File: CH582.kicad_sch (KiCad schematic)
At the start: 27 parts, among them SW1 RESET, SW2 POWER, SW3 POWER, U2 XC6220B331QR-G, U3 M3406, Y1 32MHz, Y2 Crystal_Small

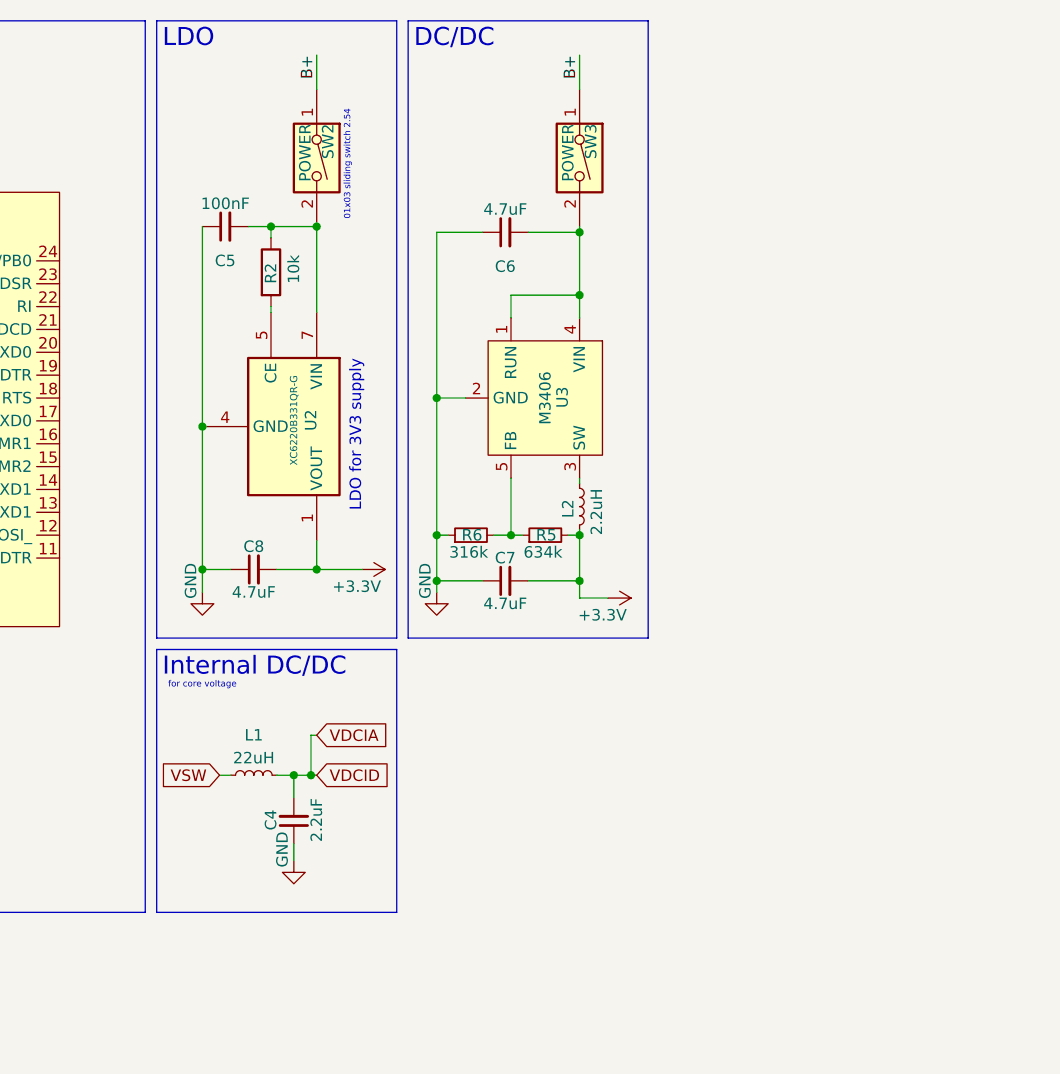
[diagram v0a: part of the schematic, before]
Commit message: added charging circuit
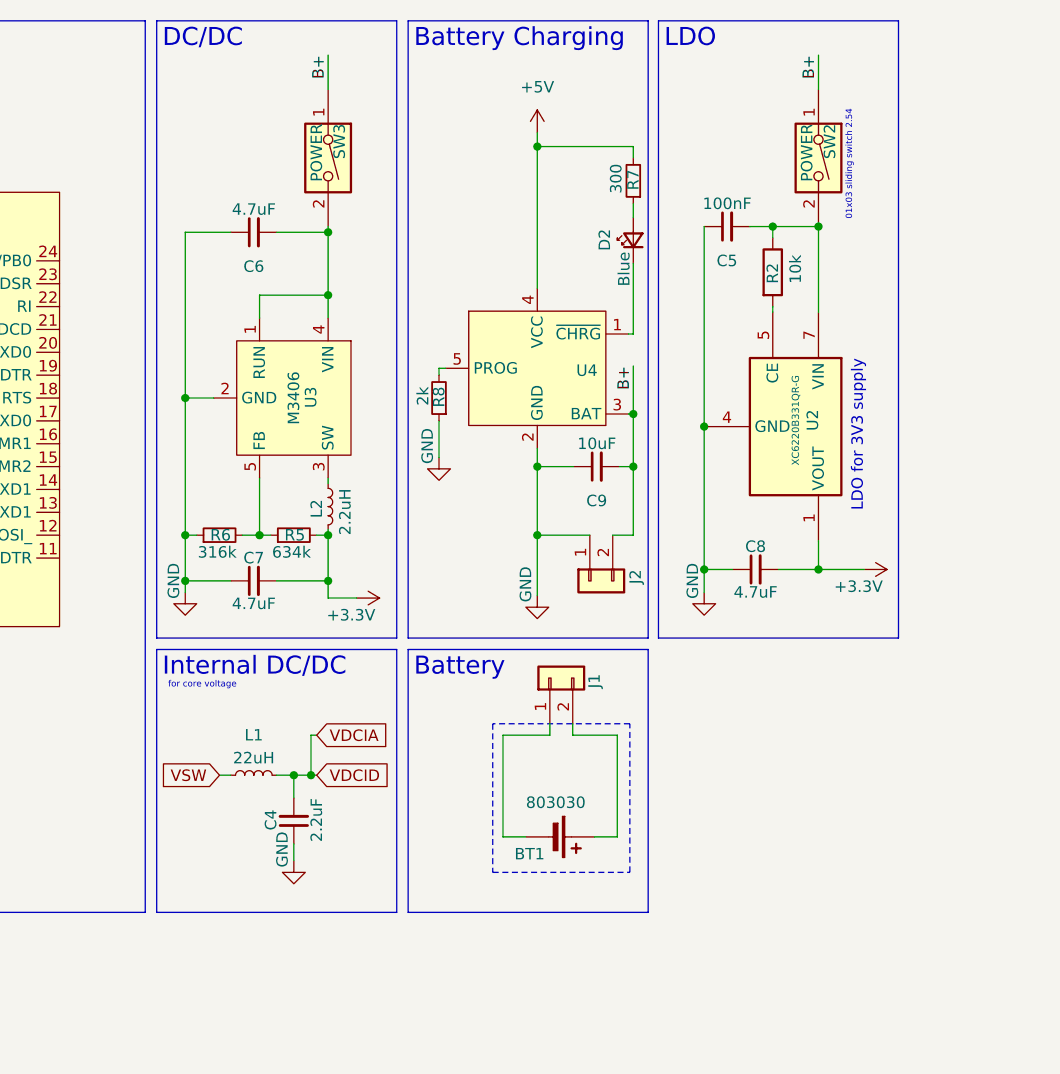
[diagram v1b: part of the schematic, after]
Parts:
- added BT1: 803030, symbol Device:Battery_Cell
- added C9: 10uF, Capacitor_SMD:C_1206_3216Metric_Pad1.33x1.80mm_HandSolder, symbol Device:C_Small
- added D2: Blue, symbol Device:LED_Small
- added J1, J2: Conn_01x02, symbol Connector_Generic:Conn_01x02
- added R7: 300, symbol Device:R_Small
- added R8: 2k, symbol Device:R_Small
- added U4: ~, symbol Custom:PJ4054B
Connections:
- net B+: now also C9.2, J2.2 (Pin_2), U4.3 (BAT)
- net GND: now also C9.1, J2.1 (Pin_1), R8.1, U4.2 (GND)
- new net: BT1.1 (+), J1.2 (Pin_2)
- new net: BT1.2 (-), J1.1 (Pin_1)
- new net: D2.2 (A), R7.1
- new net: D2.1 (K), U4.1 (~{CHRG})
- new net: R8.2, U4.5 (PROG)
- new net +5V: R7.2, U4.4 (VCC)
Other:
- note added: "Battery"
- note added: "Battery Charging"
- moved on the sheet: C5, C6, C7, C8, L2, R2, R5, R6, SW2, SW3, U2, U3

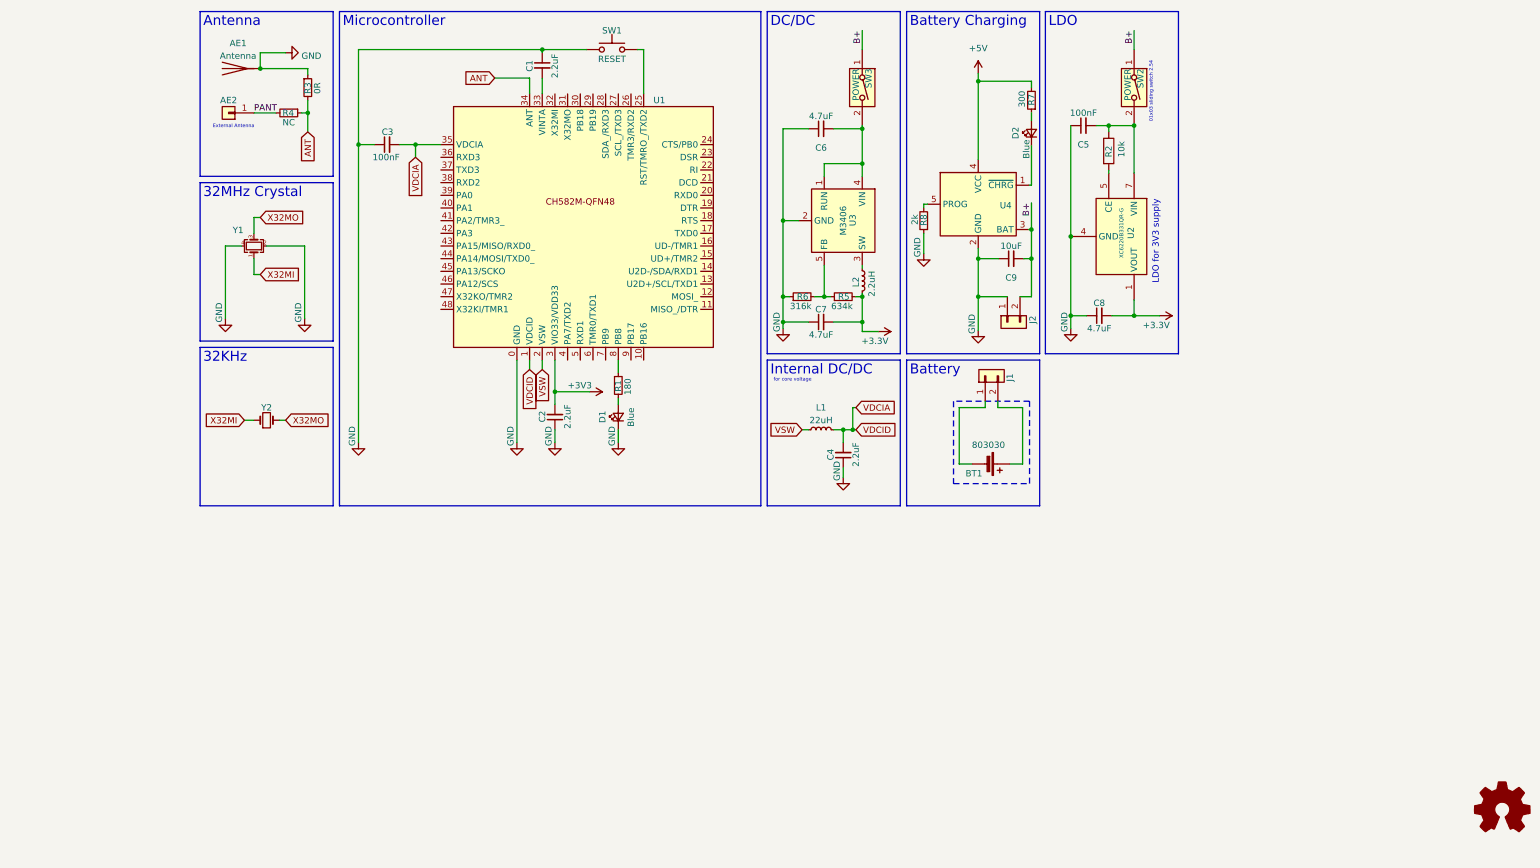
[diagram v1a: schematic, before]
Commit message: restructured layout
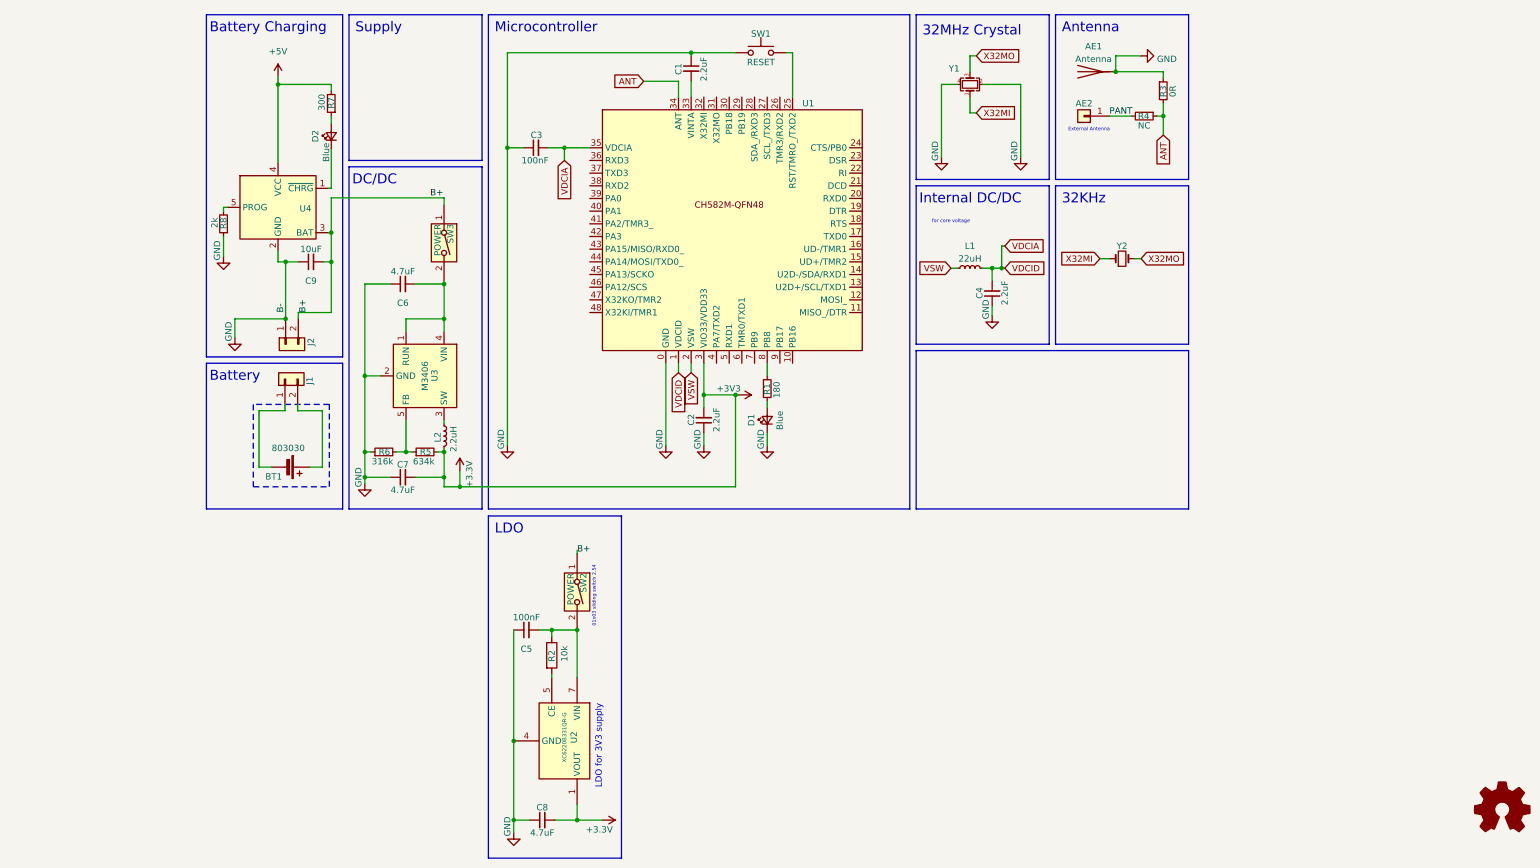
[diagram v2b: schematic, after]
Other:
- note added: "Supply"
- moved on the sheet: AE1, AE2, BT1, C1, C2, C3, C4, C5, C6, C7, C8, C9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

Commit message: Bat Lvl, GP conn, icm/lsm
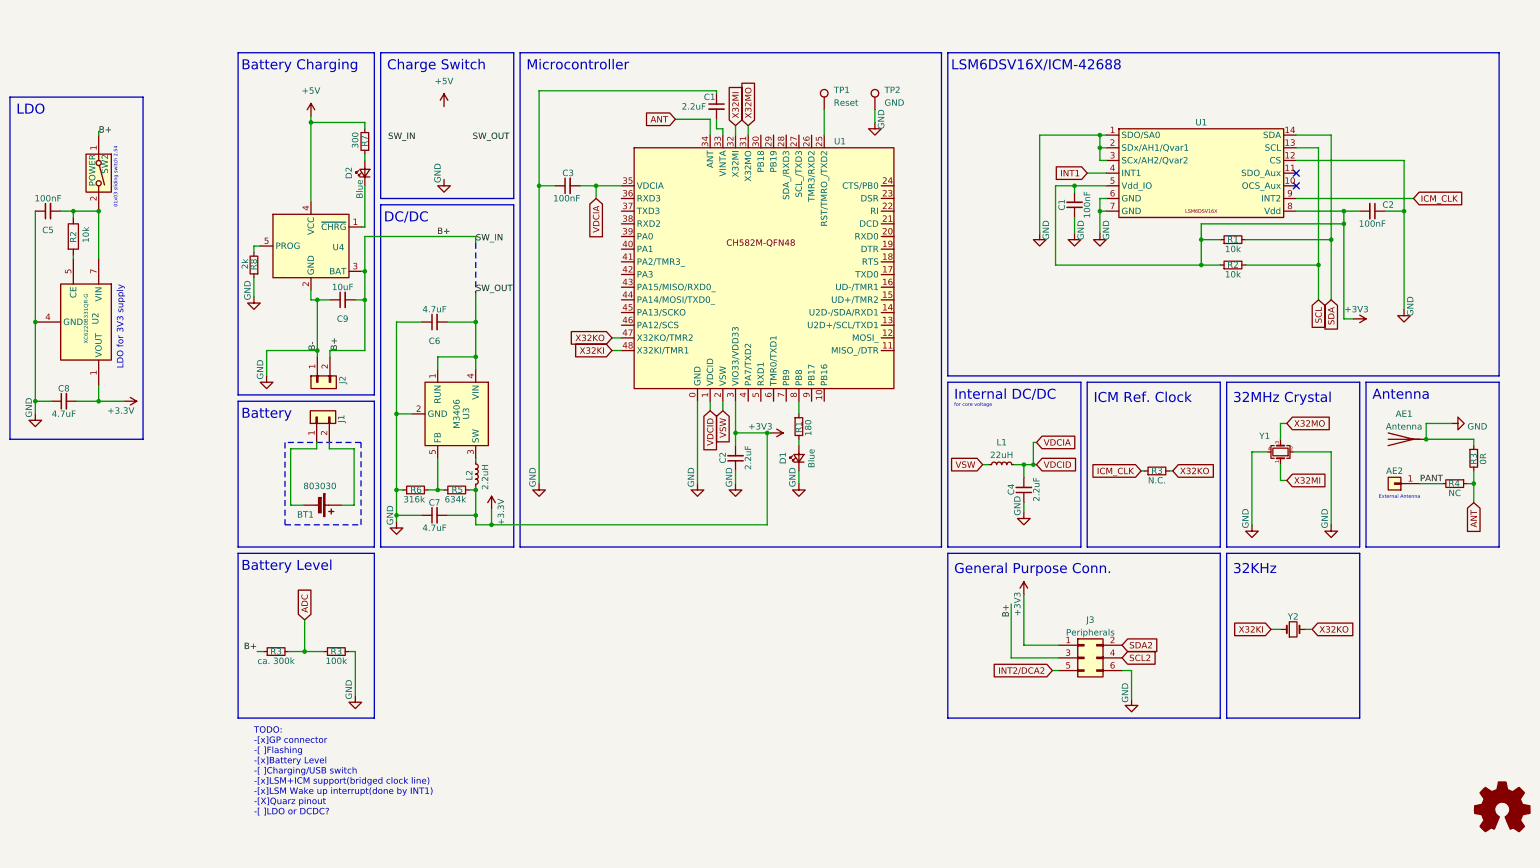
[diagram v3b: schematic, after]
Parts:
- removed SW1: RESET, symbol Switch:SW_Push
- removed SW3: POWER, Connector_PinSocket_2.54mm:PinSocket_1x03_P2.54mm_Vertical, symbol Switch:SW_DIP_x01
- added C1, C2: 100nF, Capacitor_SMD:C_0805_2012Metric_Pad1.18x1.45mm_HandSolder, symbol Device:C_Small
- added J3: Peripherals, symbol Connector_Generic:Conn_02x03_Odd_Even
- added R1, R2: 10k, Resistor_SMD:R_0805_2012Metric_Pad1.20x1.40mm_HandSolder, symbol Device:R_Small
- added R3: ca. 300k, Resistor_SMD:R_0805_2012Metric_Pad1.20x1.40mm_HandSolder, symbol Device:R_Small
- added R3: 100k, Resistor_SMD:R_0805_2012Metric_Pad1.20x1.40mm_HandSolder, symbol Device:R_Small
- added R3: N.C., Resistor_SMD:R_0805_2012Metric_Pad1.20x1.40mm_HandSolder, symbol Device:R_Small
- added TP1: Reset, symbol Connector:TestPoint
- added TP2: GND, symbol Connector:TestPoint
- added U1: ~, Package_LGA:Bosch_LGA-14_3x2.5mm_P0.5mm, symbol Custom:LSM6DSV16X
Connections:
- net +3V3: now also C1.2, C2.2, J3.1 (Pin_1), R1.1, R2.1, U1.5 (Vdd_IO), U1.8 (Vdd)
- net B+: now also J3.3 (Pin_3), R3.1
- net GND: now also C1.1, C2.1, J3.6 (Pin_6), R3.2, TP2.1, U1.1 (SDO/SA0), U1.12 (CS), U1.2 (SDx/AH1/Qvar1), U1.3 (SCx/AH2/Qvar2), U1.6 (GND), U1.7 (GND)
- net X32MI: now also U1.32 (X32MI); no longer Y2.1
- net X32MO: now also U1.31 (X32MO); no longer Y2.2
- net SW_OUT: now reaches C6.2, U3.1 (RUN), U3.4 (VIN)
- net at U1.25 (RST/TMRO_/TXD2): now also TP1.1
- net X32KO: now reaches U1.47 (X32KO/TMR2)
- net X32KO: now also Y2.2, R3.2
- net X32KI: now reaches U1.48 (X32KI/TMR1)
- net X32KI: now also Y2.1
- new net ADC: R3.1, R3.2
- new net ICM_CLK: R3.1, U1.9 (INT2)
- new net INT1: U1.4 (INT1)
- new net INT2/DCA2: J3.5 (Pin_5)
- new net SCL: R2.2, U1.13 (SCL)
- new net SCL2: J3.4 (Pin_4)
- new net SDA: R1.2, U1.14 (SDA)
- new net SDA2: J3.2 (Pin_2)
- no-connect marks 0 -> 2
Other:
- note added: "Battery Level"
- note added: "Charge Switch"
- note added: "General Purpose Conn."
- note added: "ICM Ref. Clock"
- note added: "LSM6DSV16X/ICM-42688"
- note added: "TODO: -[x]GP connector -[ ]Flashing -[x]Battery Level -[ ]Charging/USB switch -[x]LSM+ICM support(bridged clock line) -[x]LSM Wake up interrupt(done by INT1) -[X]Quarz pinout -[ ]LDO or DCDC?"
- note removed: "Supply"
- moved on the sheet: AE1, AE2, BT1, C1, C2, C3, C4, C5, C6, C7, C8, C9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

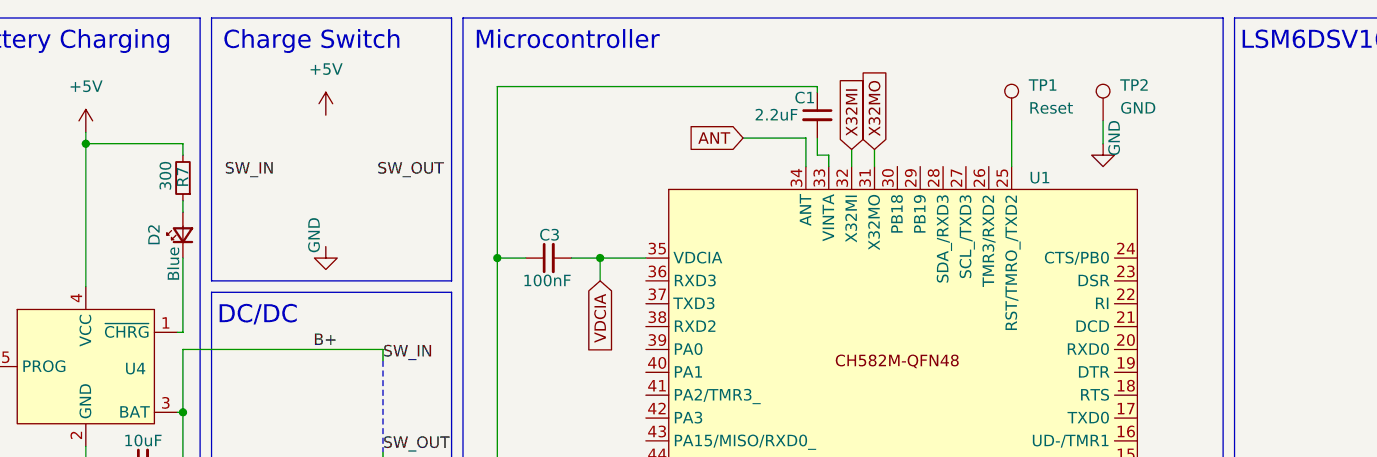
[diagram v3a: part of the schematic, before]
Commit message: added testpoints/pad reset
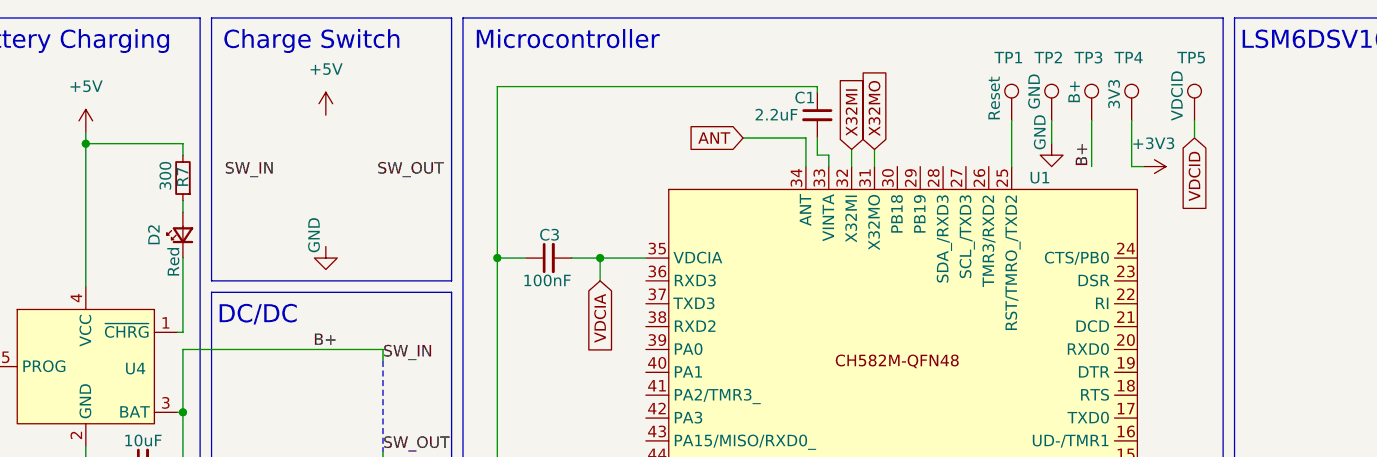
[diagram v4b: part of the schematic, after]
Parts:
- added TP3: B+, symbol Connector:TestPoint
- added TP4: 3V3, symbol Connector:TestPoint
- added TP5: VDCID, symbol Connector:TestPoint
- D2: value Blue -> Red
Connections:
- net +3V3: now also TP4.1
- net B+: now also TP3.1
- net VDCIA: now also TP5.1
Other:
- moved on the sheet: TP2
